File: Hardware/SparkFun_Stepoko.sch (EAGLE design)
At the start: 178 parts, among them J1 AVR ISP, Q1 16MHZ, Q2 100A/100V, U1 ATMEGA328, U10 +12v, U2 FT232RLSSOP, U3 74LVC1G04, U4 LM25011, U5 DRV8811, U6 74HC7014D, U7 7432SE, U8 DRV8811, U9 DRV8811

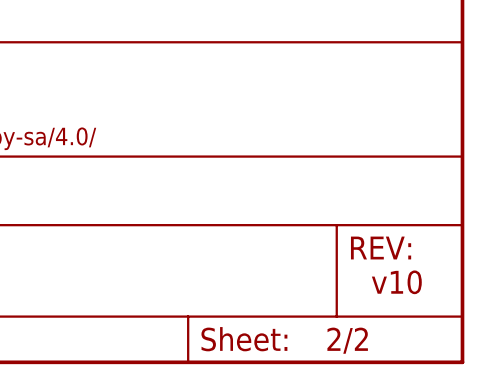
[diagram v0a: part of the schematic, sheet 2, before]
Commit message: updated current drive setting resistors
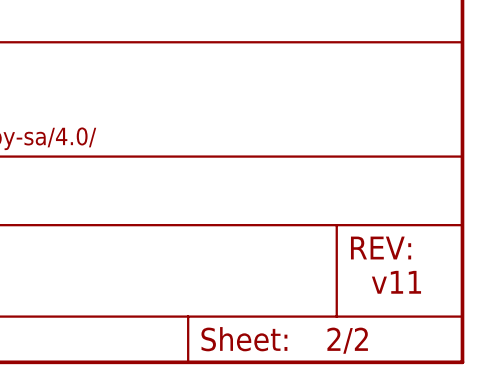
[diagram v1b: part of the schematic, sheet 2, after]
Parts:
- R16, R25, R37: value 3.3K -> 10K; device SparkFun-Resistors:3.3KOHM1/10W1%(0603) -> SparkFun-Resistors:10KOHM-1/10W-1%(0603)0603
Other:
- note added: "v11"
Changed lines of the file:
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@@
 <part name="GND6" library="SparkFun" deviceset="GND" device=""/>
 <part name="P+18" library="SparkFun" deviceset="VCC" device="" value="12V"/>
-<part name="R37" library="SparkFun-Resistors" deviceset="3.3KOHM1/10W1%(0603)" device="" value="3.3K"/>
+<part name="R37" library="SparkFun-Resistors" deviceset="10KOHM-1/10W-1%(0603)" device="0603" value="10K"/>
 <part name="GND26" library="SparkFun" deviceset="GND" device=""/>
 <part name="C44" library="SparkFun-Capacitors" deviceset="0.1UF-25V(+80/-20%)(0603)" device="" value="0.1uF"/>
@@
 <part name="C14" library="SparkFun-Capacitors" deviceset="47UF-50V-20%(ELECT)" device="" value="47uF"/>
 <part name="C15" library="SparkFun-Capacitors" deviceset="0.18UF-10V(+-10%)(0603)" device="" value="0.18uF"/>
-<part name="R16" library="SparkFun-Resistors" deviceset="3.3KOHM1/10W1%(0603)" device="" value="3.3K"/>
+<part name="R16" library="SparkFun-Resistors" deviceset="10KOHM-1/10W-1%(0603)" device="0603" value="10K"/>
 <part name="GND18" library="SparkFun" deviceset="GND" device=""/>
 <part name="C24" library="SparkFun-Capacitors" deviceset="0.1UF-25V(+80/-20%)(0603)" device="" value="0.1uF"/>
@@
 <part name="C35" library="SparkFun-Capacitors" deviceset="47UF-50V-20%(ELECT)" device="" value="47uF"/>
 <part name="C36" library="SparkFun-Capacitors" deviceset="0.18UF-10V(+-10%)(0603)" device="" value="0.18uF"/>
-<part name="R25" library="SparkFun-Resistors" deviceset="3.3KOHM1/10W1%(0603)" device="" value="3.3K"/>
+<part name="R25" library="SparkFun-Resistors" deviceset="10KOHM-1/10W-1%(0603)" device="0603" value="10K"/>
 <part name="GND31" library="SparkFun" deviceset="GND" device=""/>
 <part name="C37" library="SparkFun-Capacitors" deviceset="0.1UF-25V(+80/-20%)(0603)" device="" value="0.1uF"/>
@@
 <wire x1="284.48" y1="279.4" x2="281.94" y2="279.4" width="0.4064" layer="94"/>
 <wire x1="289.56" y1="279.4" x2="289.56" y2="0" width="0.4064" layer="97"/>
-<text x="421.64" y="7.62" size="2.54" layer="94">v10</text>
+<text x="421.64" y="7.62" size="2.54" layer="94">v11</text>
 <text x="350.52" y="10.16" size="2.54" layer="94">Casey Kuhns</text>
 <wire x1="130.81" y1="181.61" x2="133.35" y2="181.61" width="0.1524" layer="94"/>

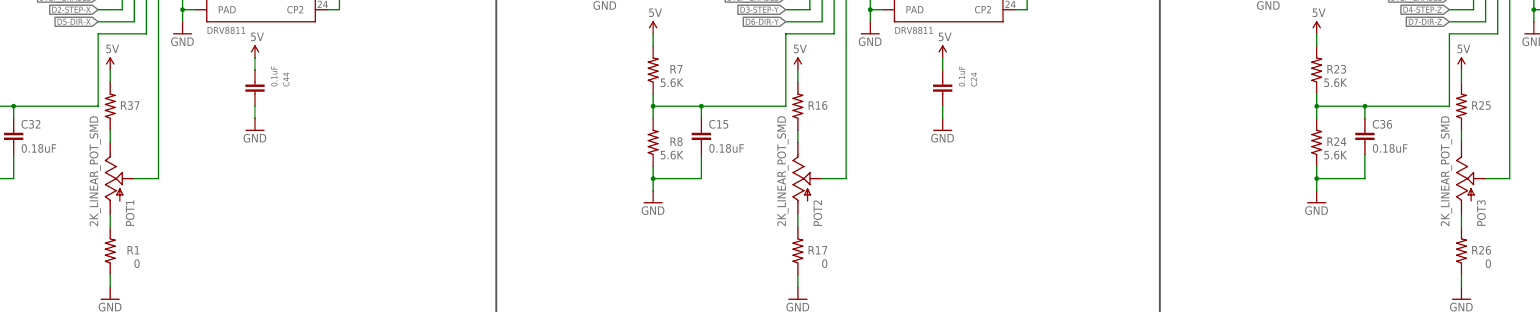
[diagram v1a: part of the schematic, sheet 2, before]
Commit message: added readme and updated to v11 hardware
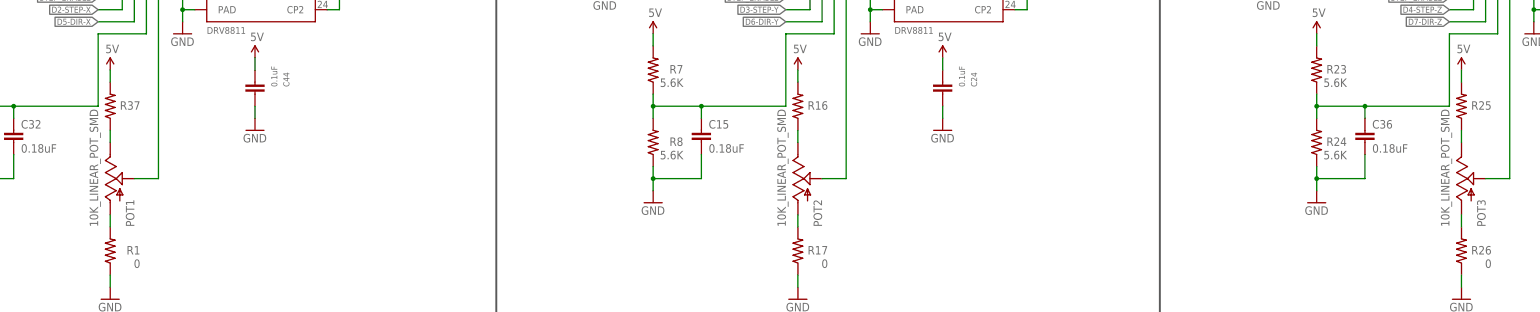
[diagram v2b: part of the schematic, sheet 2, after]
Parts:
- POT1, POT2, POT3: value 2K_LINEAR_POT_SMD -> 10K_LINEAR_POT_SMD; device SparkFun-Resistors:2K_LINEAR_POT_SMD -> SparkFun-Resistors:10K_LINEAR_POT_SMD
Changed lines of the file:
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@@
 <part name="SUPPLY3" library="SparkFun-Aesthetics" deviceset="VIN" device=""/>
 <part name="SUPPLY5" library="SparkFun-Aesthetics" deviceset="VIN" device=""/>
-<part name="POT1" library="SparkFun-Resistors" deviceset="2K_LINEAR_POT_SMD" device=""/>
+<part name="POT1" library="SparkFun-Resistors" deviceset="10K_LINEAR_POT_SMD" device=""/>
 <part name="R1" library="SparkFun-Resistors" deviceset="0OHM-1/10W-5%(0603)" device="" value="0"/>
 <part name="R6" library="SparkFun-Resistors" deviceset="10KOHM-1/10W-1%(0603)" device="0603" value="10K"/>
@@
 <part name="SUPPLY6" library="SparkFun-Aesthetics" deviceset="VIN" device=""/>
 <part name="SUPPLY7" library="SparkFun-Aesthetics" deviceset="VIN" device=""/>
-<part name="POT2" library="SparkFun-Resistors" deviceset="2K_LINEAR_POT_SMD" device=""/>
+<part name="POT2" library="SparkFun-Resistors" deviceset="10K_LINEAR_POT_SMD" device=""/>
 <part name="R17" library="SparkFun-Resistors" deviceset="0OHM-1/10W-5%(0603)" device="" value="0"/>
 <part name="Y-A" library="SparkFun-Connectors" deviceset="M02" device="3.5MM_LOCK" value="3.5mm"/>
@@
 <part name="SUPPLY35" library="SparkFun-Aesthetics" deviceset="VIN" device=""/>
 <part name="SUPPLY36" library="SparkFun-Aesthetics" deviceset="VIN" device=""/>
-<part name="POT3" library="SparkFun-Resistors" deviceset="2K_LINEAR_POT_SMD" device=""/>
+<part name="POT3" library="SparkFun-Resistors" deviceset="10K_LINEAR_POT_SMD" device=""/>
 <part name="R26" library="SparkFun-Resistors" deviceset="0OHM-1/10W-5%(0603)" device="" value="0"/>
 <part name="Z-A" library="SparkFun-Connectors" deviceset="M02" device="3.5MM_LOCK" value="3.5mm"/>

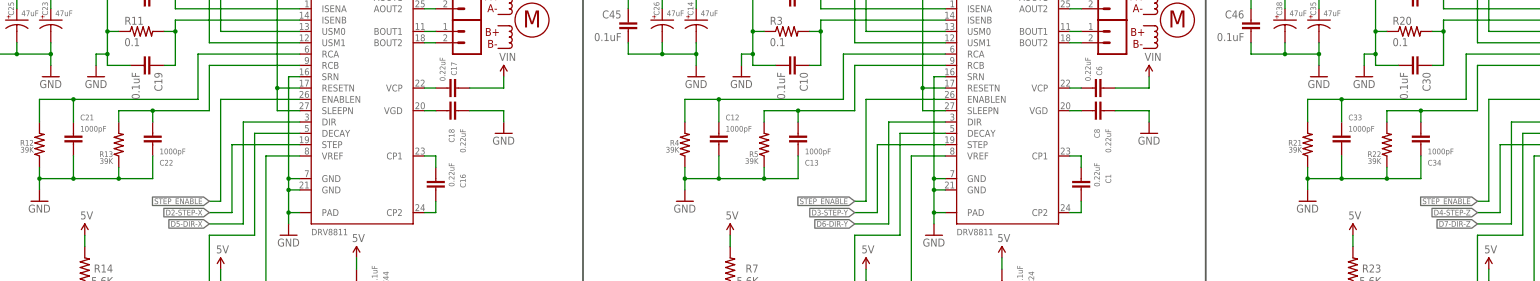
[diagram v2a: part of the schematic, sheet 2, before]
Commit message: Replaced 25v cap with 100v cap
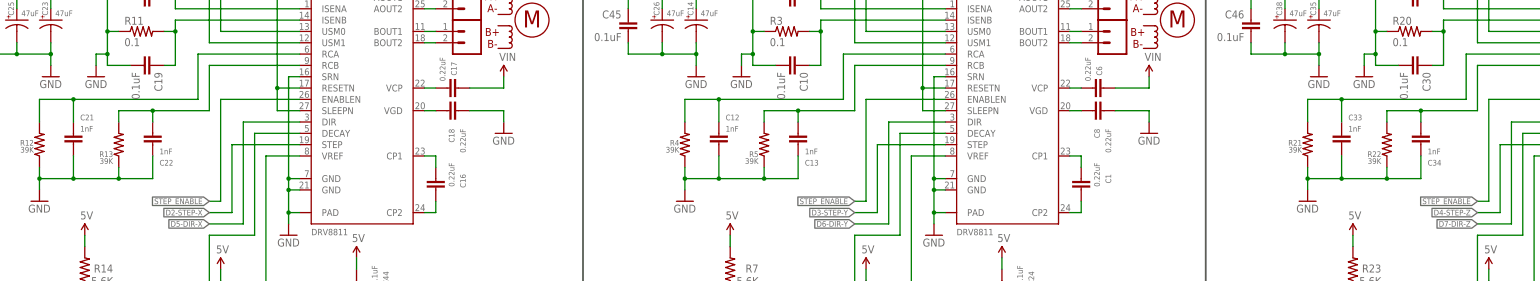
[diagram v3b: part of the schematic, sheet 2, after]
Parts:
- C12, C13, C21, C22, C33, C34: value 1000pF -> 1nF
- C43, C45, C46: device SparkFun-Capacitors:0.1UF-25V(+80/-20%)(0603) -> SparkFun-Capacitors:0.1UF-100V-10%(0603)
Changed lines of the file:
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@@
 <part name="R11" library="SparkFun-Resistors" deviceset="0.1OHM-1/2W-1%(1210)" device="" value="0.1"/>
 <part name="R12" library="SparkFun-Resistors" deviceset="39KOHM-1/10W-1%(0603)" device="" value="39K"/>
-<part name="C21" library="SparkFun-Capacitors" deviceset="1NF/1000PF-50V-10%(0603)" device="" value="1000pF"/>
+<part name="C21" library="SparkFun-Capacitors" deviceset="1NF/1000PF-50V-10%(0603)" device="" value="1nF"/>
 <part name="R13" library="SparkFun-Resistors" deviceset="39KOHM-1/10W-1%(0603)" device="" value="39K"/>
-<part name="C22" library="SparkFun-Capacitors" deviceset="1NF/1000PF-50V-10%(0603)" device="" value="1000pF"/>
+<part name="C22" library="SparkFun-Capacitors" deviceset="1NF/1000PF-50V-10%(0603)" device="" value="1nF"/>
 <part name="R14" library="SparkFun-Resistors" deviceset="5.6KOHM-1/10W-1%(0603)" device="" value="5.6K"/>
 <part name="R15" library="SparkFun-Resistors" deviceset="5.6KOHM-1/10W-1%(0603)" device="" value="5.6K"/>
@@
 <part name="R3" library="SparkFun-Resistors" deviceset="0.1OHM-1/2W-1%(1210)" device="" value="0.1"/>
 <part name="R4" library="SparkFun-Resistors" deviceset="39KOHM-1/10W-1%(0603)" device="" value="39K"/>
-<part name="C12" library="SparkFun-Capacitors" deviceset="1NF/1000PF-50V-10%(0603)" device="" value="1000pF"/>
+<part name="C12" library="SparkFun-Capacitors" deviceset="1NF/1000PF-50V-10%(0603)" device="" value="1nF"/>
 <part name="R5" library="SparkFun-Resistors" deviceset="39KOHM-1/10W-1%(0603)" device="" value="39K"/>
-<part name="C13" library="SparkFun-Capacitors" deviceset="1NF/1000PF-50V-10%(0603)" device="" value="1000pF"/>
+<part name="C13" library="SparkFun-Capacitors" deviceset="1NF/1000PF-50V-10%(0603)" device="" value="1nF"/>
 <part name="R7" library="SparkFun-Resistors" deviceset="5.6KOHM-1/10W-1%(0603)" device="" value="5.6K"/>
 <part name="R8" library="SparkFun-Resistors" deviceset="5.6KOHM-1/10W-1%(0603)" device="" value="5.6K"/>
@@
 <part name="R20" library="SparkFun-Resistors" deviceset="0.1OHM-1/2W-1%(1210)" device="" value="0.1"/>
 <part name="R21" library="SparkFun-Resistors" deviceset="39KOHM-1/10W-1%(0603)" device="" value="39K"/>
-<part name="C33" library="SparkFun-Capacitors" deviceset="1NF/1000PF-50V-10%(0603)" device="" value="1000pF"/>
+<part name="C33" library="SparkFun-Capacitors" deviceset="1NF/1000PF-50V-10%(0603)" device="" value="1nF"/>
 <part name="R22" library="SparkFun-Resistors" deviceset="39KOHM-1/10W-1%(0603)" device="" value="39K"/>
-<part name="C34" library="SparkFun-Capacitors" deviceset="1NF/1000PF-50V-10%(0603)" device="" value="1000pF"/>
+<part name="C34" library="SparkFun-Capacitors" deviceset="1NF/1000PF-50V-10%(0603)" device="" value="1nF"/>
 <part name="R23" library="SparkFun-Resistors" deviceset="5.6KOHM-1/10W-1%(0603)" device="" value="5.6K"/>
 <part name="R24" library="SparkFun-Resistors" deviceset="5.6KOHM-1/10W-1%(0603)" device="" value="5.6K"/>
@@
 <part name="SUPPLY16" library="SparkFun-Aesthetics" deviceset="5V" device=""/>
 <part name="GND67" library="SparkFun" deviceset="GND" device=""/>
-<part name="C43" library="SparkFun-Capacitors" deviceset="0.1UF-25V(+80/-20%)(0603)" device="" value="0.1uF"/>
-<part name="C45" library="SparkFun-Capacitors" deviceset="0.1UF-25V(+80/-20%)(0603)" device="" value="0.1uF"/>
-<part name="C46" library="SparkFun-Capacitors" deviceset="0.1UF-25V(+80/-20%)(0603)" device="" value="0.1uF"/>
+<part name="C43" library="SparkFun-Capacitors" deviceset="0.1UF-100V-10%(0603)" device="" value="0.1uF"/>
+<part name="C45" library="SparkFun-Capacitors" deviceset="0.1UF-100V-10%(0603)" device="" value="0.1uF"/>
+<part name="C46" library="SparkFun-Capacitors" deviceset="0.1UF-100V-10%(0603)" device="" value="0.1uF"/>
 <part name="FID1" library="SparkFun-Aesthetics" deviceset="FIDUCIAL" device="1X2"/>
 <part name="FID2" library="SparkFun-Aesthetics" deviceset="FIDUCIAL" device="1X2"/>
